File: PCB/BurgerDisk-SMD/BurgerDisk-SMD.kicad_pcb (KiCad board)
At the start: 2 copper layers, 65.1 x 96.9 mm, 23 parts, among them J1 Daisy port out, J2 2-pin header, J3 ICSP_ISP6, J4 Daisy port in, J5 MicroSD module, U1 PC817C-S, U2 ATmega328P-AU, Y1 Resonator_GND2

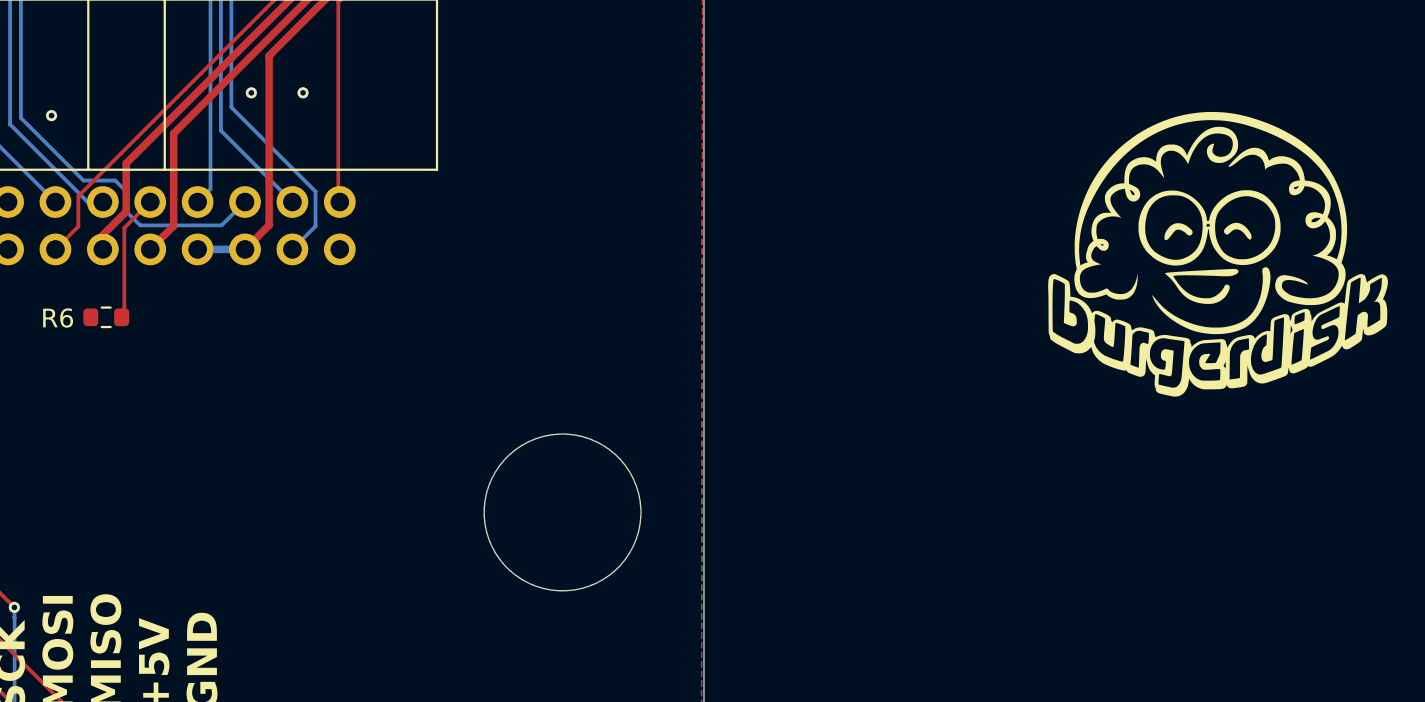
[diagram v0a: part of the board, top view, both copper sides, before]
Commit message: Put the logo back on the PCB
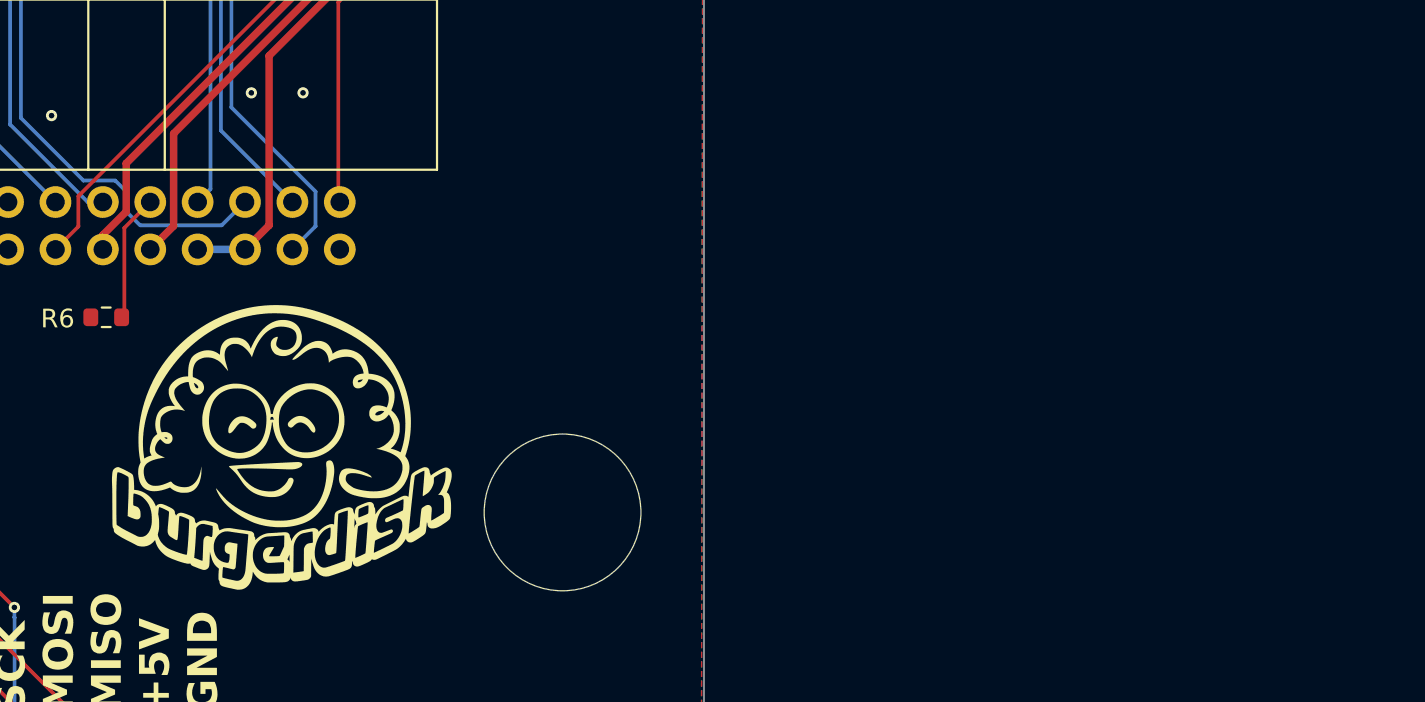
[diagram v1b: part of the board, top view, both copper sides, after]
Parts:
- moved G*** 51.2 mm to (142.0, 120.7)
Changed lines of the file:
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@@
 	(footprint "LOGO"
 		(layer "F.Cu")
-		(at 192.162905 110.299597)
+		(at 141.986 120.65)
 		(property "Reference" "G***"
 			(at 0 0 0)

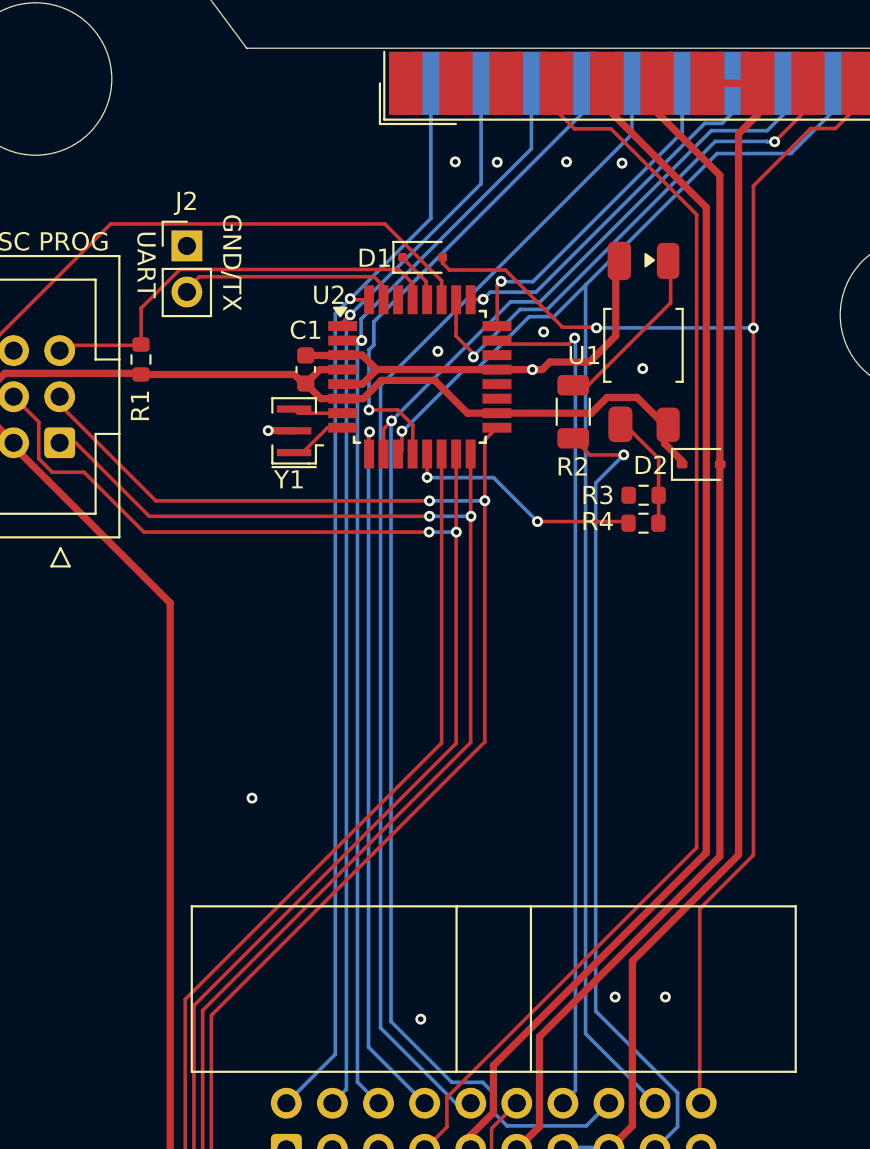
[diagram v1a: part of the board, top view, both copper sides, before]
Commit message: Move to bigger pads for diodes
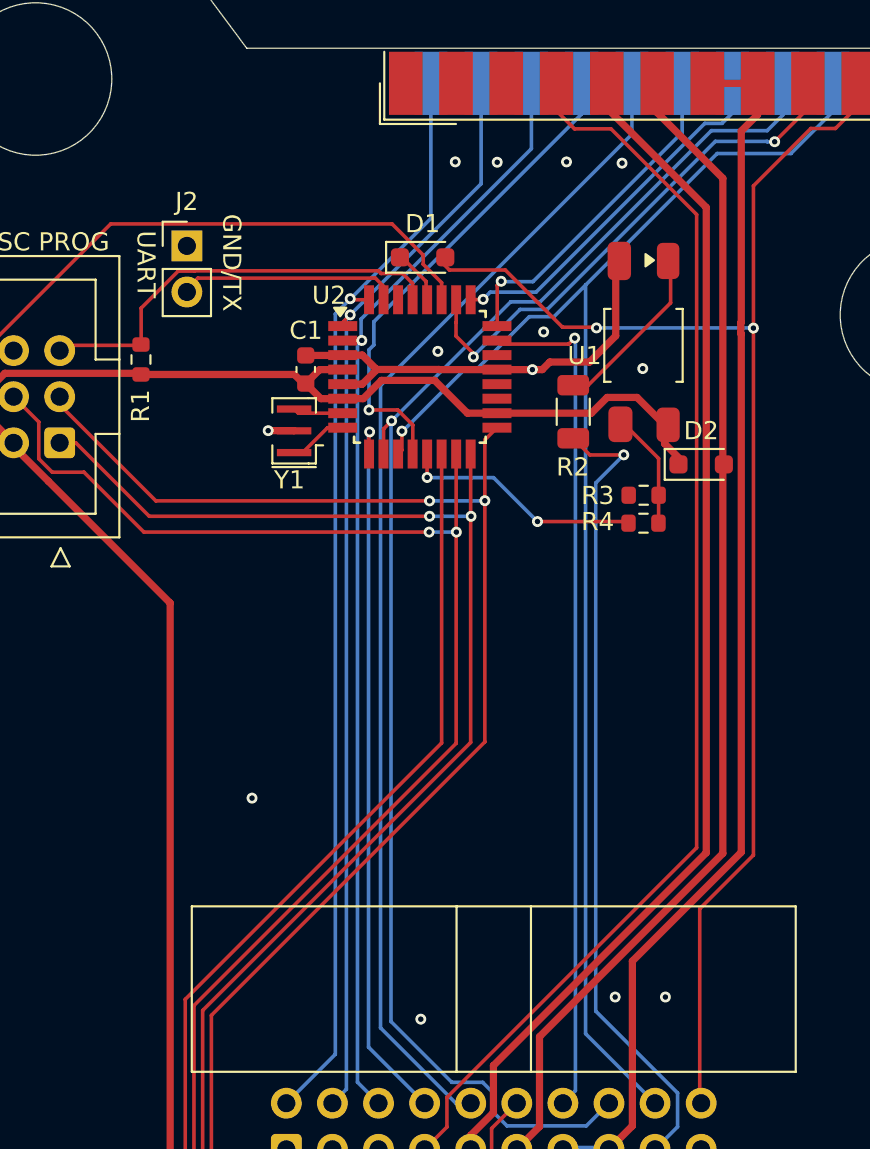
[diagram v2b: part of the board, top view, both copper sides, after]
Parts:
- D1: footprint Diode_SMD:D_SOD-323F -> Diode_SMD:D_SOD-323_HandSoldering
- D2: footprint Diode_SMD:D_SOD-323 -> Diode_SMD:D_SOD-323_HandSoldering
